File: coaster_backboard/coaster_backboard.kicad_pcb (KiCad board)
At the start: 2 copper layers, 93 x 93 mm, 83 parts, among them J1 USB, P1 TC2030, U1 STM32F072C8Tx, U2 IS31FL3733-QF

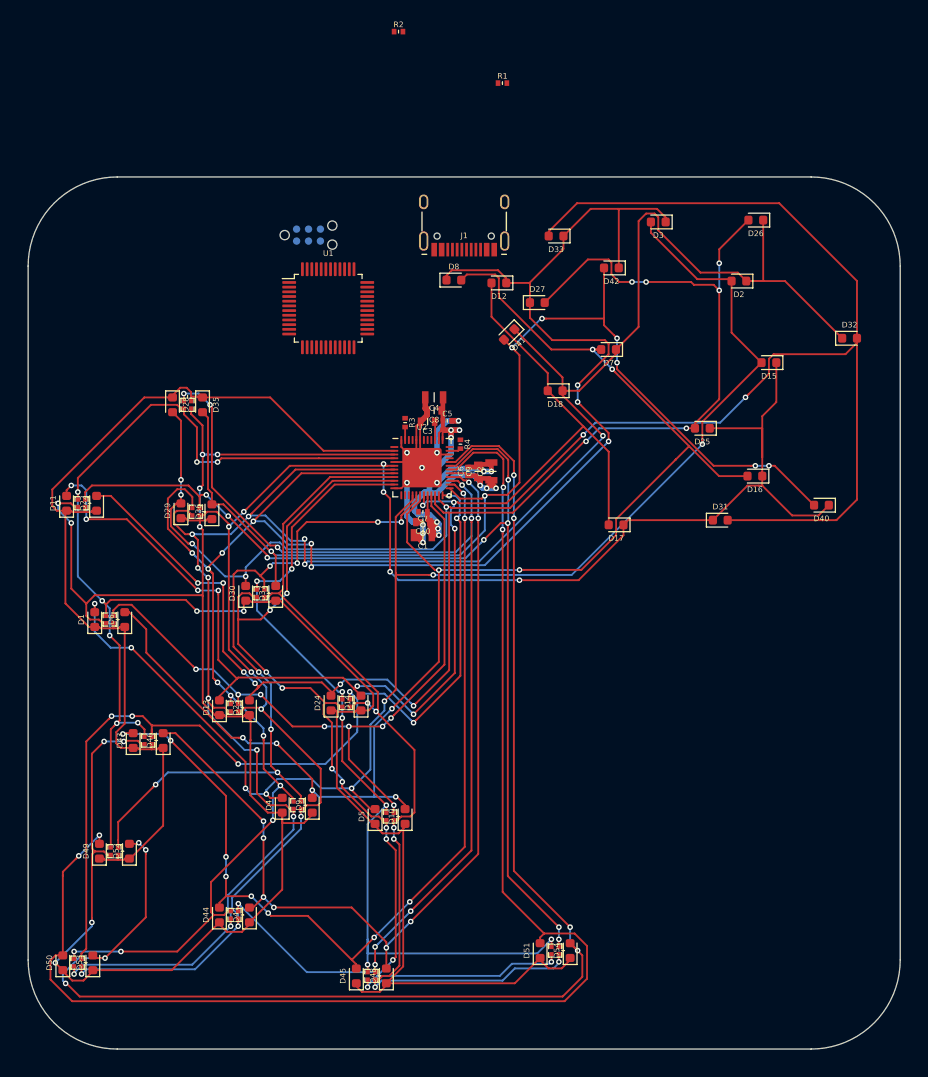
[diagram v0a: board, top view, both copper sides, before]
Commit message: routing 80%
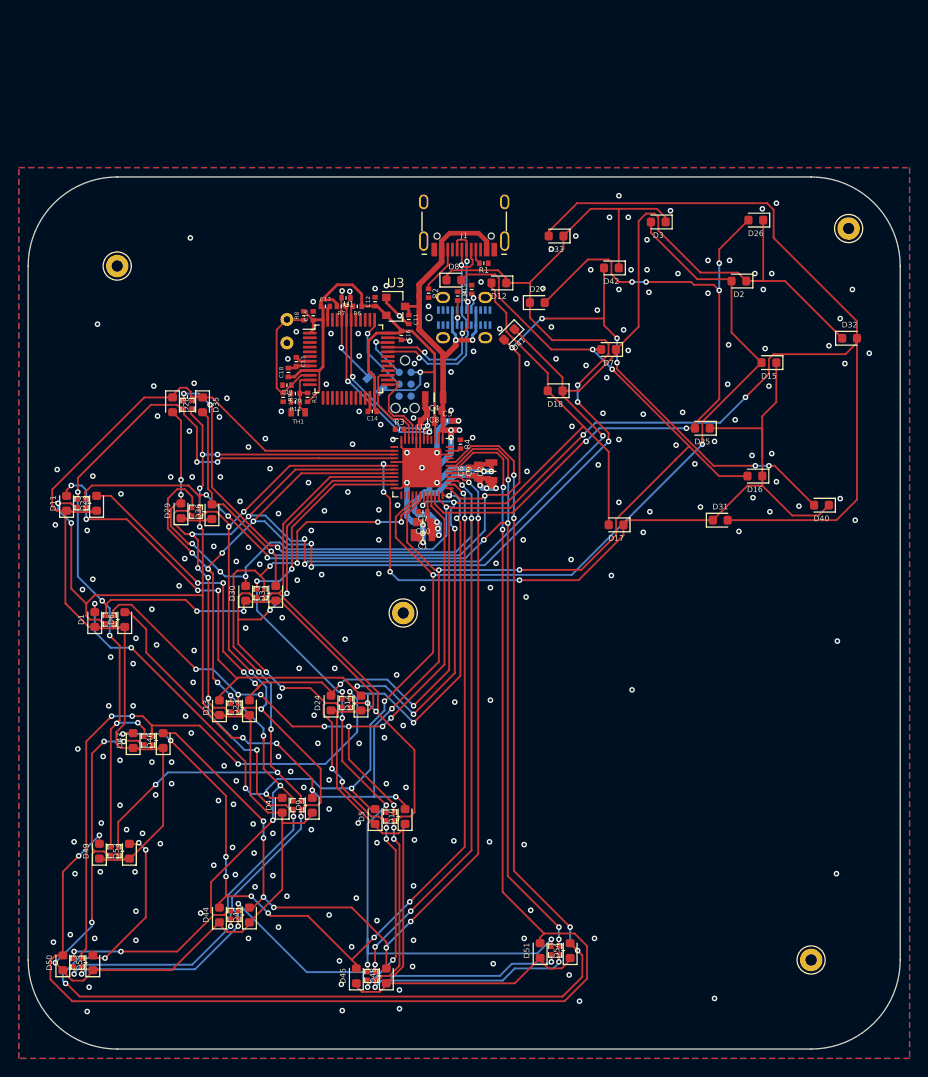
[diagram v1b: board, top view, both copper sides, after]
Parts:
- added C11: 100n, otter:C_0402, F.Cu at (90.6, 65.2)
- added C12: 100n, otter:C_0402, F.Cu at (87.0, 63.3)
- added C13: 100n, otter:C_0402, F.Cu at (78.6, 69.7)
- added C14: 100n, otter:C_0402, F.Cu at (86.7, 75.0)
- added C15: 100n, otter:C_0402, F.Cu at (80.4, 64.8)
- added C16: 100n, otter:C_0402, F.Cu at (89.8, 66.9)
- added C17: 100n, otter:C_0402, F.Cu at (81.7, 63.8)
- added C18: 100n, otter:C_0402, F.Cu at (77.8, 70.8)
- added C19: 100n, otter:C_0402, F.Cu at (77.6, 72.2)
- added C20: 100n, otter:C_0402, F.Cu at (78.5, 73.1)
- added J2: MP, Connector_Pin:Pin_D1.0mm_L10.0mm_LooseFit, F.Cu at (137.5, 55.5)
- added J3: MP, Connector_Pin:Pin_D1.0mm_L10.0mm_LooseFit, F.Cu at (90.0, 96.5)
- added J4: MP, Connector_Pin:Pin_D1.0mm_L10.0mm_LooseFit, F.Cu at (133.5, 133.5)
- added J5: MP, Connector_Pin:Pin_D1.0mm_L10.0mm_LooseFit, F.Cu at (59.5, 59.5)
- added J6: Solderpad, Connector_Pin:Pin_D0.7mm_L6.5mm_W1.8mm_FlatFork, B.Cu at (77.6, 65.2)
- added J7: Solderpad, Connector_Pin:Pin_D0.7mm_L6.5mm_W1.8mm_FlatFork, B.Cu at (77.6, 67.7)
- added J8: USB, otter:918-418K2022Y40004, B.Cu at (96.5, 65.0)
- added JP1: DFU, otter:R_0805, B.Cu at (87.0, 72.0)
- added R10: 5k1, otter:R_0402, F.Cu at (79.8, 73.5)
- added R11: 5k1, otter:R_0402, F.Cu at (78.5, 74.0)
- added R14: 5k1, otter:R_0402, F.Cu at (95.8, 62.7)
- added R15: 5k1, otter:R_0402, F.Cu at (97.3, 62.0)
- added R5: 5k1, otter:R_0402, F.Cu at (83.9, 62.9)
- added R6: 5k1, otter:R_0402, F.Cu at (85.1, 63.8)
- added R7: 5k1, otter:R_0402, F.Cu at (83.4, 63.8)
- added R8: 5k1, otter:R_0402, F.Cu at (79.4, 64.8)
- added R9: 5k1, otter:R_0402, F.Cu at (77.2, 73.5)
- added TH1: NTC, otter:R_0603, F.Cu at (78.8, 75.1)
- added U3: MCP1700-3302E_SOT23, Package_TO_SOT_SMD:SOT-23, F.Cu at (89.2, 63.8)
- moved R2 28.1 mm to (92.7, 62.4), turned to 270 degrees
- moved R1 19.3 mm to (98.6, 59.2), turned to 180 degrees
- moved P1 18.9 mm to (90.2, 72.1), turned to 270 degrees
- moved U1 5.83 mm to (84.2, 69.4)
- moved R3 0.92 mm to (89.6, 76.9), turned to 0 degrees
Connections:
- U1 pad 10: Net-(U1-Pad10) -> NTC1
- U1 pad 11: Net-(U1-Pad11) -> NTC0
- U1 pad 26: Net-(U1-Pad26) -> INT
- U1 pad 27: Net-(U1-Pad27) -> SDB
- U1 pad 32: Net-(U1-Pad32) -> D-
- U1 pad 33: Net-(U1-Pad33) -> D+
- U1 pad 34: Net-(U1-Pad34) -> SWDIO
- U1 pad 37: Net-(U1-Pad37) -> SWCLK
- U1 pad 42: Net-(U1-Pad42) -> SCL
- U1 pad 43: Net-(U1-Pad43) -> SDA
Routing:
- net +3V3: track 1.97 -> 68.0 mm, vias 0 -> 1
- net VBUS: track 50.1 -> 89.9 mm, vias 9 -> 11
- net D+: track 0.00 -> 25.2 mm, vias 0 -> 4
- net D-: track 0.00 -> 24.1 mm, vias 0 -> 2
- net SDA: track 0.00 -> 20.0 mm, vias 0 -> 2
- net SCL: track 0.00 -> 19.9 mm, vias 0 -> 2
- net NTC1: track 0.00 -> 14.1 mm
- net GND: track 54.6 -> 67.2 mm, vias 11 -> 245
- net Net-(JP1-Pad1): track 0.00 -> 10.5 mm, vias 0 -> 2
- net SDB: track 0.00 -> 9.79 mm
- net INT: track 0.00 -> 9.32 mm
- net SWCLK: track 0.00 -> 8.57 mm, vias 0 -> 1
- net SWDIO: track 0.00 -> 5.53 mm, vias 0 -> 1
- net NTC0: track 0.00 -> 5.53 mm
- net Net-(J1-PadB5): track 0.00 -> 5.04 mm
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- added copper zone on B.Cu, net GND
- added copper zone on F.Cu, net GND
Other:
- board text added: "Designed by Jana Marie Inspired by @FredTemperton based on the works of @kani_aji_"
- board text removed: "Designed by @JanHenrikH Inspired by @FredTemperton based on the works of @kani_aji_"
- board text removed: "TODO: Zweite Stehende USB buchse"

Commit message: updated hw
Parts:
- added D64: White, LED_SMD:LED_0603_1608Metric, F.Cu at (127.6, 54.5)
- added D65: White, LED_SMD:LED_0603_1608Metric, F.Cu at (104.3, 63.4)
- added D66: Blue, LED_SMD:LED_0603_1608Metric, F.Cu at (96.6, 129.2)
- added D67: White, LED_SMD:LED_0603_1608Metric, F.Cu at (123.8, 86.6)
- added D68: White, LED_SMD:LED_0603_1608Metric, F.Cu at (137.7, 67.2)
- added D69: White, LED_SMD:LED_0603_1608Metric, F.Cu at (106.3, 56.5)
- added D70: Pink, LED_SMD:LED_0603_1608Metric, F.Cu at (72.0, 133.8)
- added D71: White, LED_SMD:LED_0603_1608Metric, F.Cu at (134.7, 85.0)
- added D72: White, LED_SMD:LED_0603_1608Metric, F.Cu at (101.2, 66.8)
- added D73: White, LED_SMD:LED_0603_1608Metric, F.Cu at (112.2, 59.6)
- added D74: Blue, LED_SMD:LED_0603_1608Metric, F.Cu at (75.2, 133.8)
- added D75: Pink, LED_SMD:LED_0603_1608Metric, F.Cu at (106.8, 134.6)
- added D76: Blue, LED_SMD:LED_0603_1608Metric, F.Cu at (110.0, 134.6)
- added D77: Pink, LED_SMD:LED_0603_1608Metric, F.Cu at (54.0, 134.2)
- added D78: Blue, LED_SMD:LED_0603_1608Metric, F.Cu at (57.2, 134.2)
- added G***: LOGO, otter:shark_girl_kani_aji__text_all, B.Cu at (95.4, 97.7)
- D12, D2, D3, D7, D8: value White -> RGBA_P1; footprint LED_SMD:LED_0603_1608Metric -> otter:FC-B1010RGBT-HG
- D18, D41: value White -> Pink
- D31: value White -> Blue
- J1: footprint otter:USB-C 16Pin -> otter:USB-C 16Pin InBoard
- moved D2 86.5 mm to (85.0, 137.4), turned to 0 degrees
- moved D12 85.5 mm to (55.6, 134.2), turned to 0 degrees
- moved D3 77.6 mm to (95.0, 129.2), turned to 0 degrees
- moved D7 75.8 mm to (73.6, 133.8), turned to 0 degrees
- moved D8 74.7 mm to (108.4, 134.6)
- moved D18 68.5 mm to (83.4, 137.4), turned to 90 degrees
- moved D31 63.0 mm to (86.6, 137.4), turned to 90 degrees
- moved D41 62.9 mm to (93.4, 129.2), turned to 90 degrees
- moved D40 41.7 mm to (100.2, 61.4)
- moved D17 32.5 mm to (117.2, 54.9)
- moved D32 31.9 mm to (112.7, 87.2), turned to 180 degrees
- moved D51 22.1 mm to (88.6, 117.3)
- moved D54 22.1 mm to (91.8, 117.3)
- moved D63 22.1 mm to (90.2, 117.3)
- moved D16 20.9 mm to (125.7, 61.0)
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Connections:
- D12 pad 1: RGBS6 -> RGBC14
- D12 pad 2: RGBC4 -> RGBS12
- D16 pad 1: RGBS4 -> RGBS5
- D16 pad 2: RGBC3 -> RGBC1
- D17 pad 1: RGBS4 -> RGBS6
- D17 pad 2: RGBC4 -> RGBC1
- D18 pad 1: RGBS5 -> RGBS7
- D18 pad 2: RGBC4 -> RGBC1
- D2 pad 1: RGBS5 -> RGBC2
- D2 pad 2: RGBC1 -> RGBS12
- D25 pad 2: RGBC6 -> RGBC3
- D26 pad 2: RGBC6 -> RGBC3
- D27 pad 2: RGBC6 -> RGBC3
- D3 pad 1: RGBS6 -> RGBC5
- D3 pad 2: RGBC1 -> RGBS12
- D31 pad 1: RGBS4 -> RGBS7
- D31 pad 2: RGBC7 -> RGBC3
- D32 pad 1: RGBS5 -> RGBS4
- D32 pad 2: RGBC7 -> RGBC4
- D33 pad 1: RGBS6 -> RGBS5
- D33 pad 2: RGBC7 -> RGBC4
- D40 pad 1: RGBS4 -> RGBS6
- D40 pad 2: RGBC9 -> RGBC4
- D41 pad 1: RGBS5 -> RGBS7
- D41 pad 2: RGBC9 -> RGBC4
- D42 pad 1: RGBS6 -> RGBS4
- D42 pad 2: RGBC9 -> RGBC6
- D7 pad 1: RGBS5 -> RGBC8
- D7 pad 2: RGBC3 -> RGBS12
- D8 pad 1: RGBS6 -> RGBC11
- D8 pad 2: RGBC3 -> RGBS12
- U2 pad 13: Net-(U2-Pad13) -> RGBS10
- U2 pad 14: Net-(U2-Pad14) -> RGBS11
- U2 pad 15: Net-(U2-Pad15) -> RGBS12
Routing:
- net RGBS11: track 0.00 -> 141.0 mm, vias 0 -> 6
- net RGBS12: track 0.00 -> 125.1 mm, vias 0 -> 10
- net RGBS10: track 0.00 -> 124.0 mm, vias 0 -> 10
- net RGBS7: track 100.0 -> 161.6 mm, vias 6 -> 17
- net RGBC9: track 124.9 -> 178.8 mm, vias 8 -> 16
- net RGBC10: track 101.1 -> 147.0 mm, vias 10 -> 8
- net RGBC7: track 181.4 -> 227.2 mm
- net RGBC14: track 114.2 -> 155.9 mm, vias 8 -> 14
- net RGBC13: track 147.2 -> 115.8 mm, vias 4 -> 6
- net RGBC2: track 77.1 -> 107.5 mm, vias 8 -> 16
- net RGBS6: track 214.7 -> 184.6 mm, vias 16 -> 10
- net RGBS3: track 193.6 -> 163.8 mm, vias 9 -> 11
- net RGBC1: track 151.8 -> 181.1 mm
- net RGBS5: track 227.2 -> 198.2 mm
- net RGBC15: track 148.2 -> 119.4 mm, vias 8 -> 10
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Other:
- outline, holes or cut-outs redrawn
- net class Default removed
- board text added: "qr code https://twitter.com/_Jana_Marie"
- board text removed: "qr code https://twitter.com/JanHenrikH"
